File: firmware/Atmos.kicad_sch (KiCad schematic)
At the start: 61 parts, among them J1 AS3935 breakout, J2 BME280 breakout, J3 USB_C_Receptacle_USB2.0_16P, J4 Micro_SD_Card, J5 Solar power input, J6 Conn_Coaxial, Q1 PMOS_Substrate, Q2 PMOS_Substrate, Q3 PMOS_Substrate, SW2 SW_Push, U1 ESP32-S3-WROOM-1, U10 TPS22918DBVR, U11 MAX17048G_T10, U12 CN3791, U13 SGP40-D-R4, U2 AP2112K-3.3, U3 DS3231M, U4 PMS5003, U5 LTC4412xS6, U7 RFM95W-915S2, U8 USBLC6-2SC6, U9 TPS61023DRLR

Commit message: TPS progress
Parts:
- added R14: 750k, symbol Device:R_US
- added R15: 100k, symbol Device:R_US
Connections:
- net SW_BOOST is gone; now on net +VBATT: L2.2
- net +5V: now also R14.2
- net FB_BOOST: now also R14.1, R15.1
- net GND: now also R15.2
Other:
- moved on the sheet: C15, R13

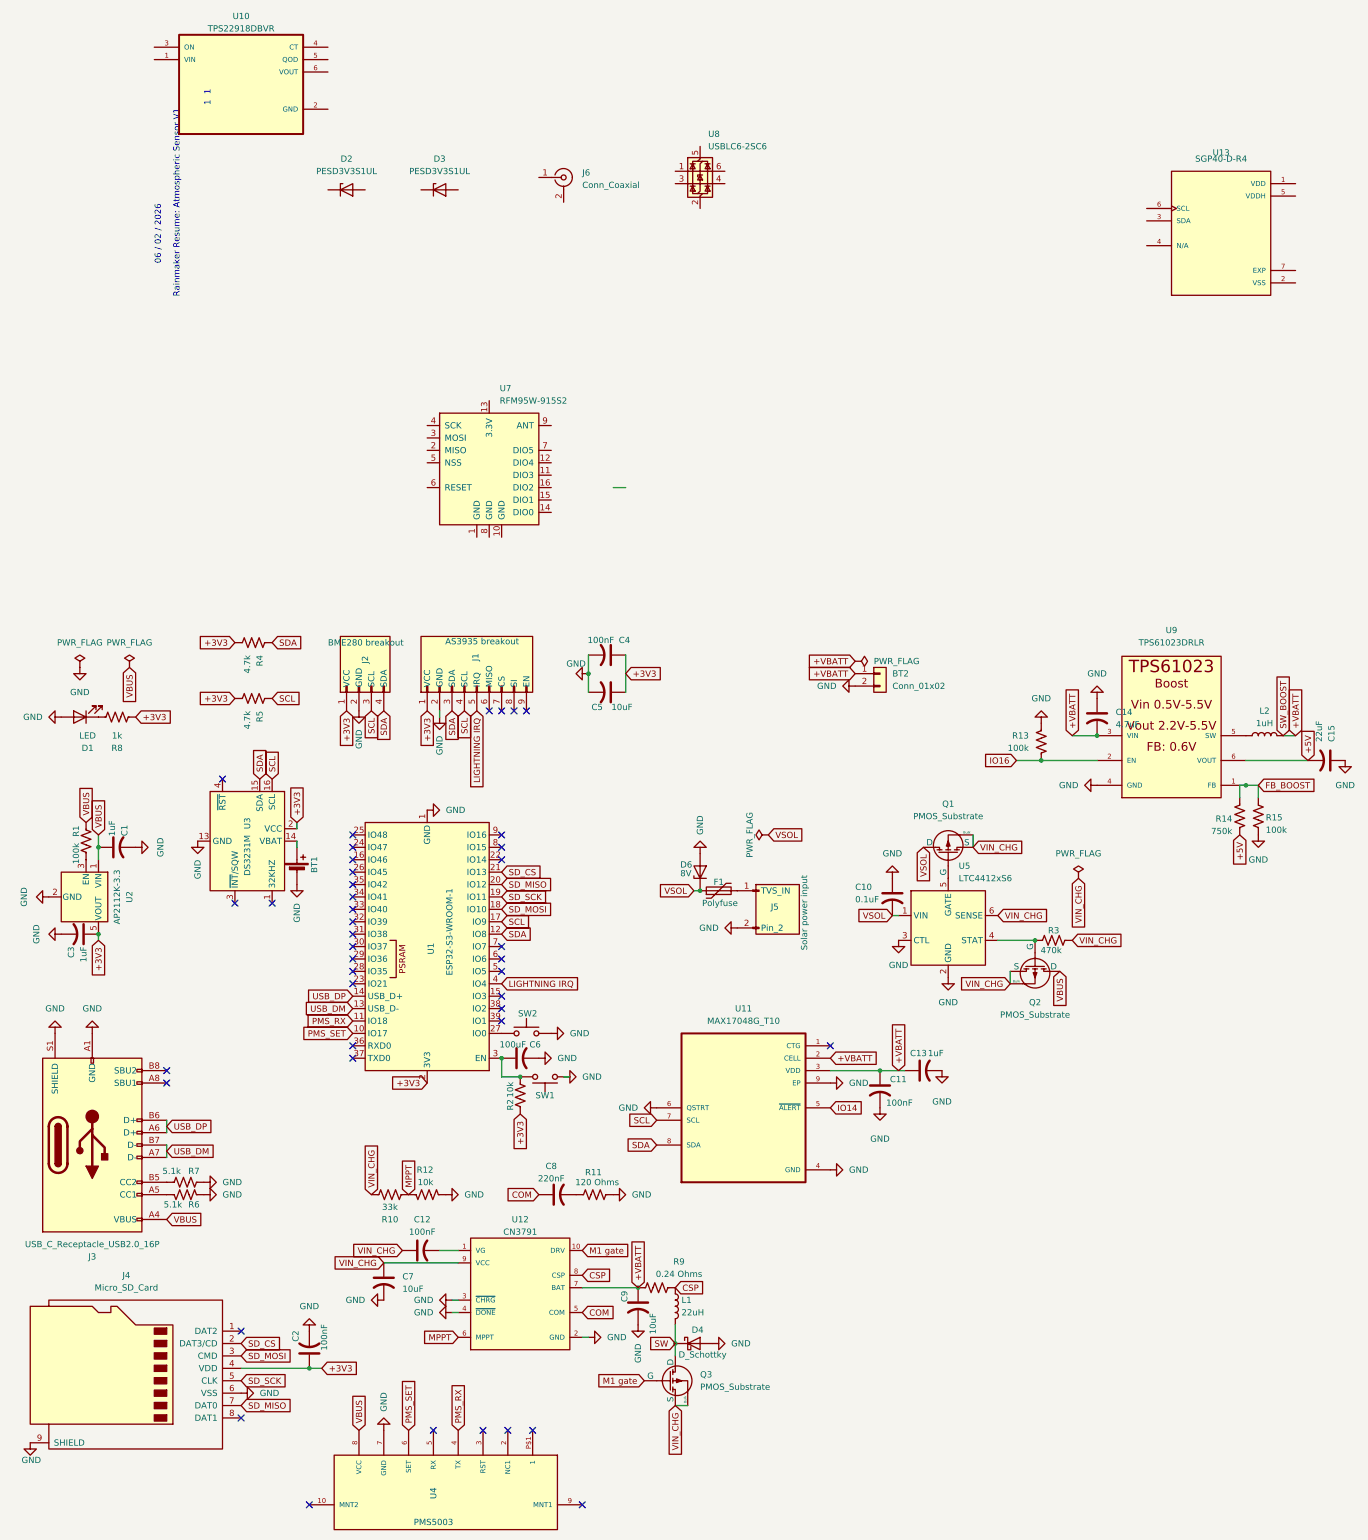
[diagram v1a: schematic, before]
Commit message: TPS finished
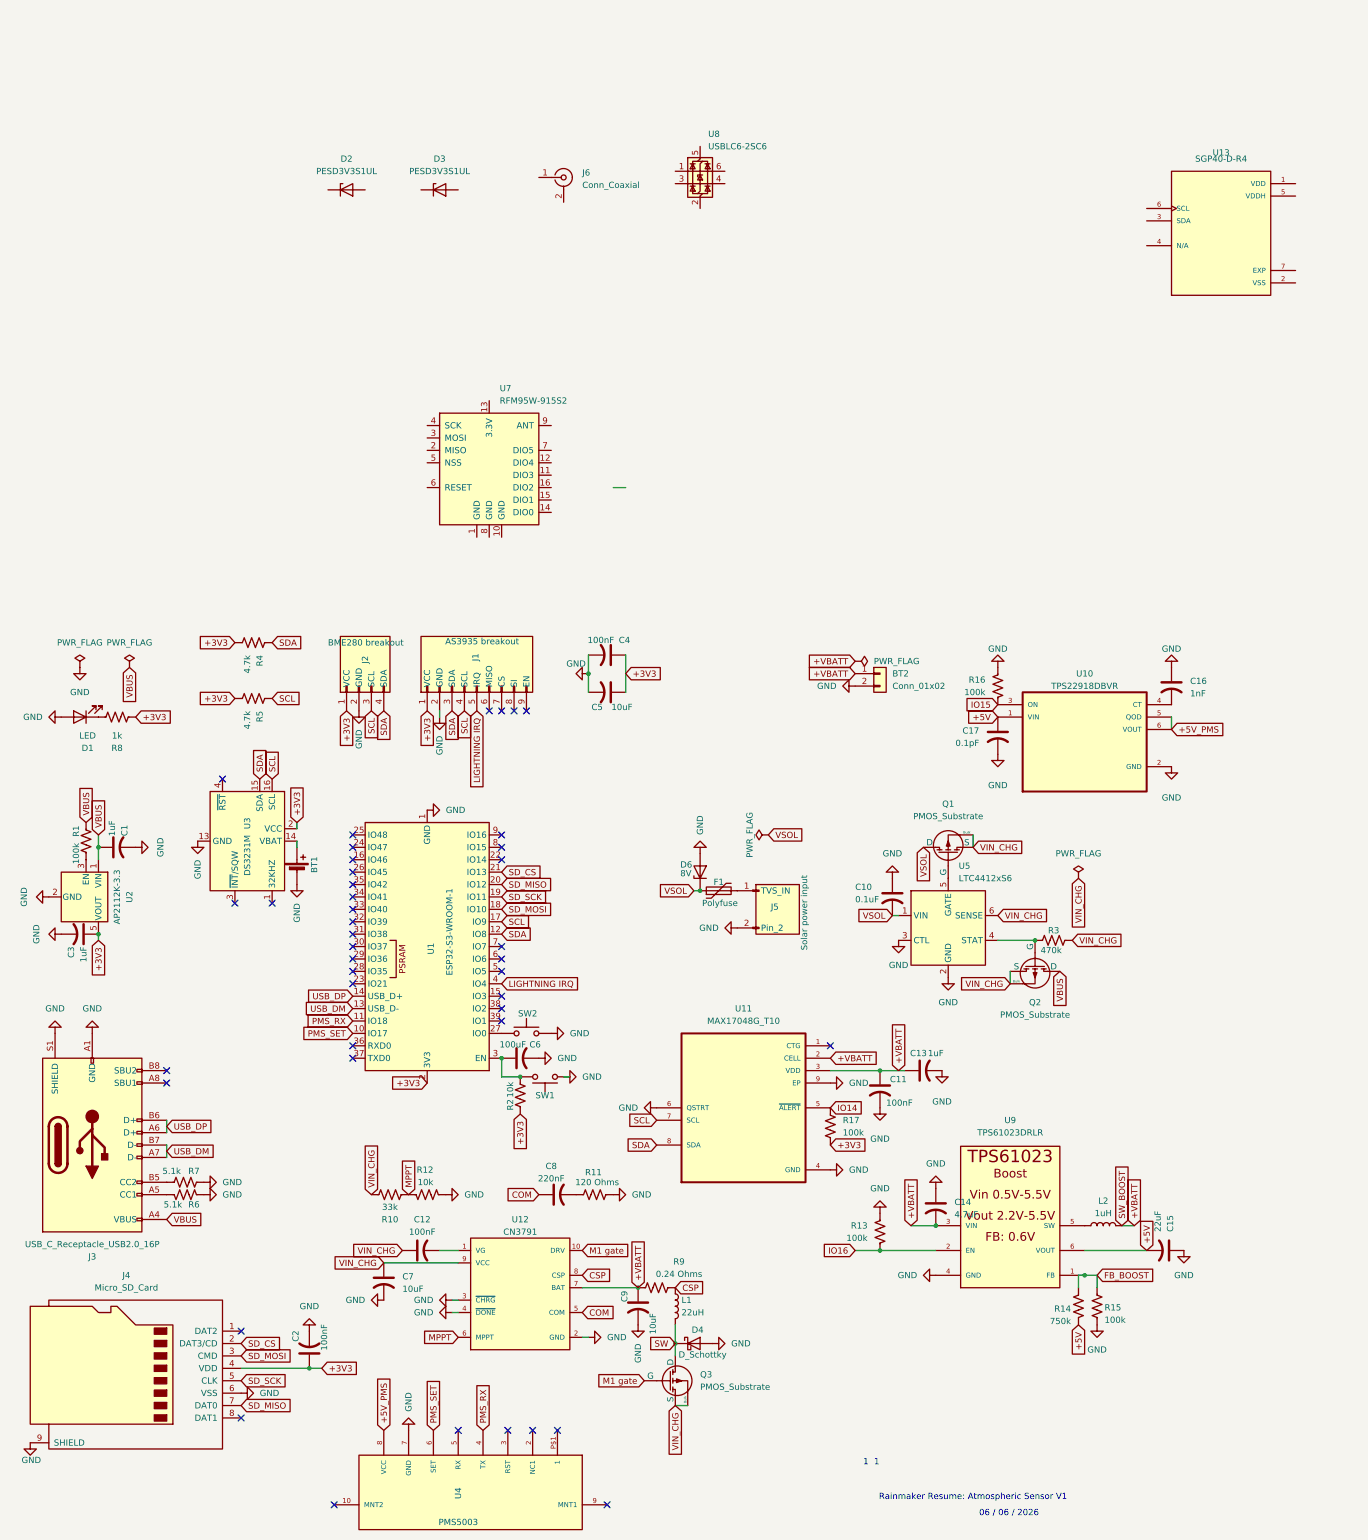
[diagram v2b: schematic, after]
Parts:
- added C16: 1nF, symbol Device:C_US
- added C17: 0.1pF, symbol Device:C_US
- added R16, R17: 100k, symbol Device:R_US
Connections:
- net +3V3: now also R17.2
- net +5V: now also U10.1 (VIN), C17.1
- net GND: now also U10.2 (GND), C16.1, C17.2, R16.1
- net IO14: now also R17.1
- net VBUS: no longer U4.8 (VCC)
- net IO15: now reaches U10.3 (ON)
- net IO15: now also R16.2
- net at U10.4 (CT): now also C16.2
- net +5V_PMS: now reaches U10.5 (QOD)
- net +5V_PMS: now also U10.6 (VOUT), U4.8 (VCC)
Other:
- note added: "06 / 06 / 2026"
- note removed: "06 / 02 / 2026"
- moved on the sheet: C14, C15, L2, R13, R14, R15, U10, U4, U9

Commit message: RF component + Antenna
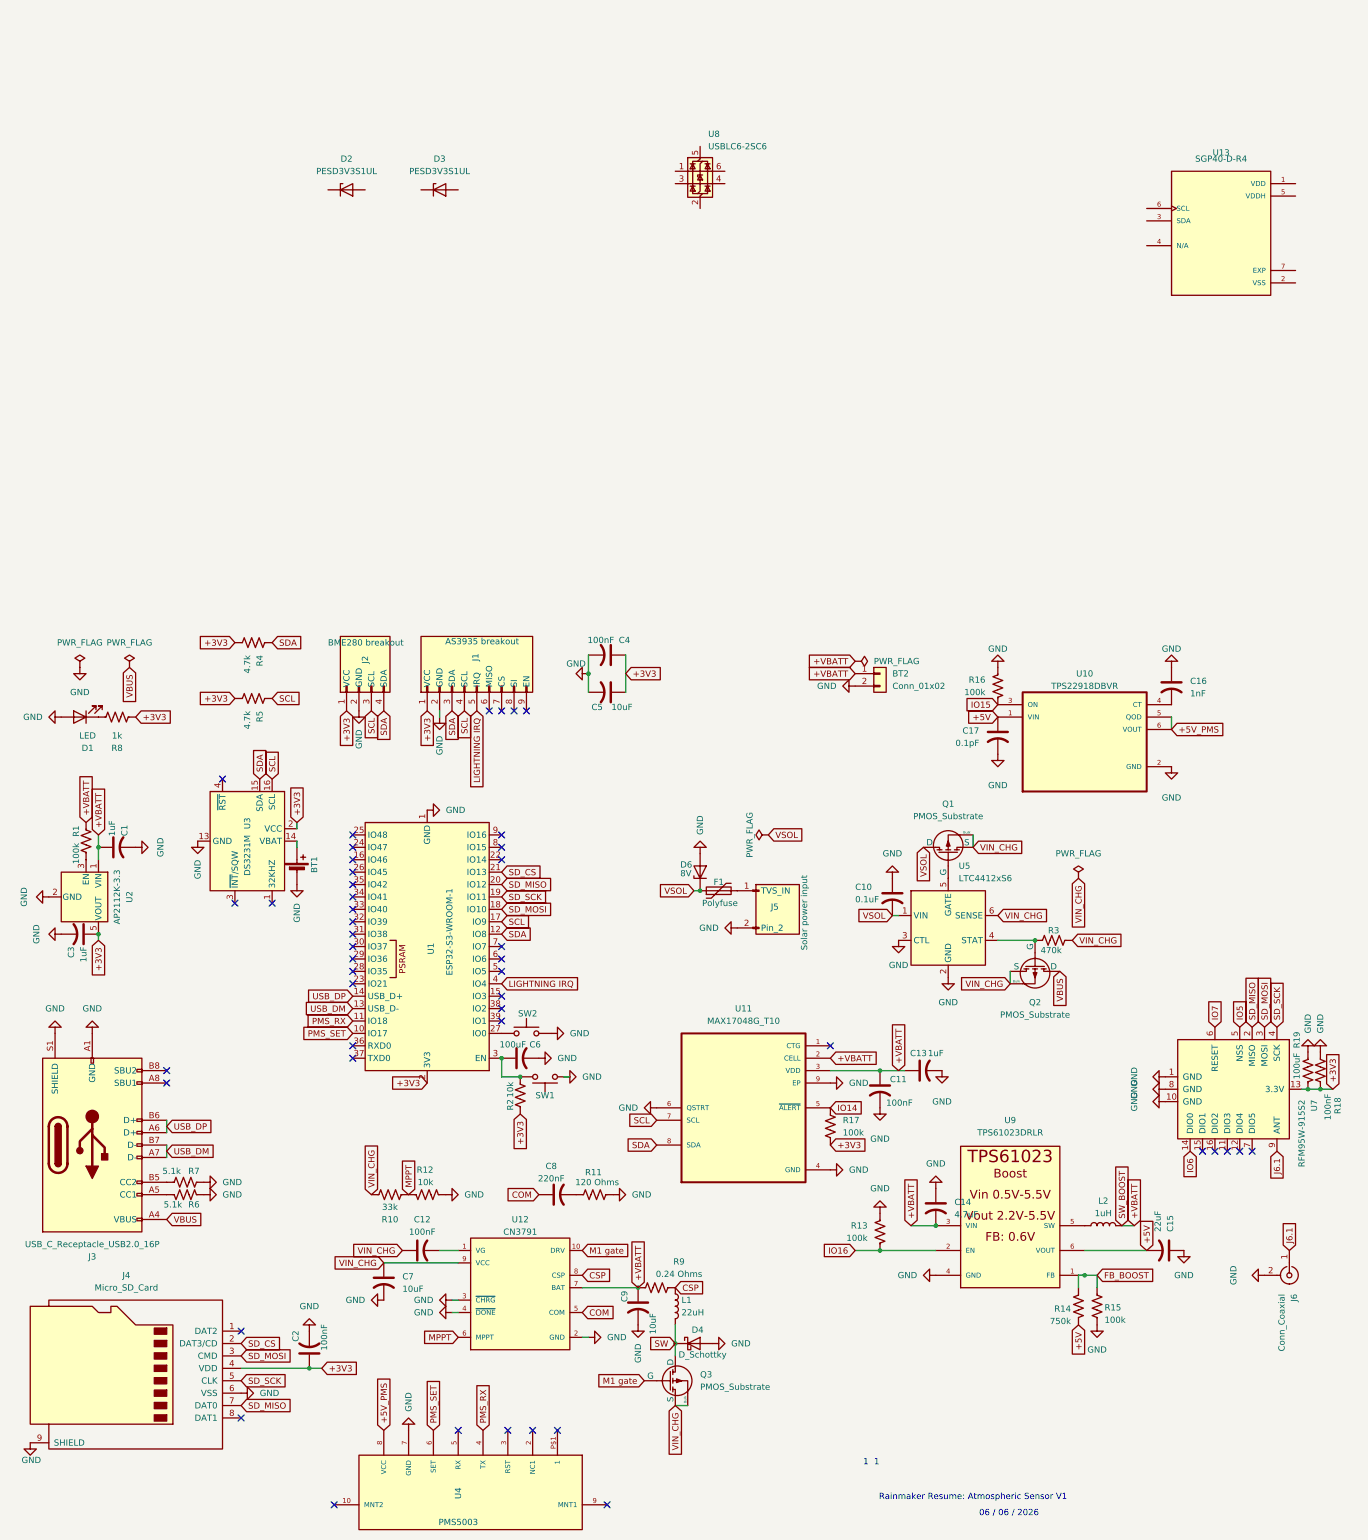
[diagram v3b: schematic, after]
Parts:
- added R18: 100nF, symbol Device:R_US
- added R19: 100uF, symbol Device:R_US
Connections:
- net +3V3: now also U7.13 (3.3V), R18.2, R19.2
- net +VBATT: now also C1.1, R1.1, U2.1 (VIN)
- net GND: now also J6.2 (Ext), U7.1 (GND), U7.10 (GND), U7.8 (GND), R18.1, R19.1
- net SD_MISO: now also U7.2 (MISO)
- net SD_MOSI: now also U7.3 (MOSI)
- net SD_SCK: now also U7.4 (SCK)
- net VBUS: no longer C1.1, R1.1, U2.1 (VIN)
- net J6.1: now reaches J6.1 (In)
- net J6.1: now also U7.9 (ANT)
- net IO6: now reaches U7.14 (DIO0)
- net IO5: now reaches U7.5 (NSS)
- net IO7: now reaches U7.6 (RESET)
- no-connect marks 42 -> 47
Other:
- moved on the sheet: J6, U7

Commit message: USBLC6 done
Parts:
- removed R18: 100nF, symbol Device:R_US
- removed R19: 100uF, symbol Device:R_US
- added C18: 100uF, symbol Device:C_Small_US
- added C19: 10uF, symbol Device:C_Small_US
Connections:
- net +3V3: now also C18.2, C19.2
- net GND: now also U8.2 (GND), C18.1, C19.1
- net USB_DM: now also U8.3 (I/O2), U8.4 (I/O2)
- net USB_DP: now also U8.1 (I/O1), U8.6 (I/O1)
- net VBUS: now also U8.5 (VBUS)
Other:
- moved on the sheet: U8
